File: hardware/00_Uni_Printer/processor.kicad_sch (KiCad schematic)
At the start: 31 parts, among them IC2 MT25QL256ABA1EW7-0SIT_TR, U1 STM32H743VIT6, U4 TLE9251VSJ, U7 LTC2862CS8-1#PBF, Y1 ABM7-25.000MHZ-D2Y-T

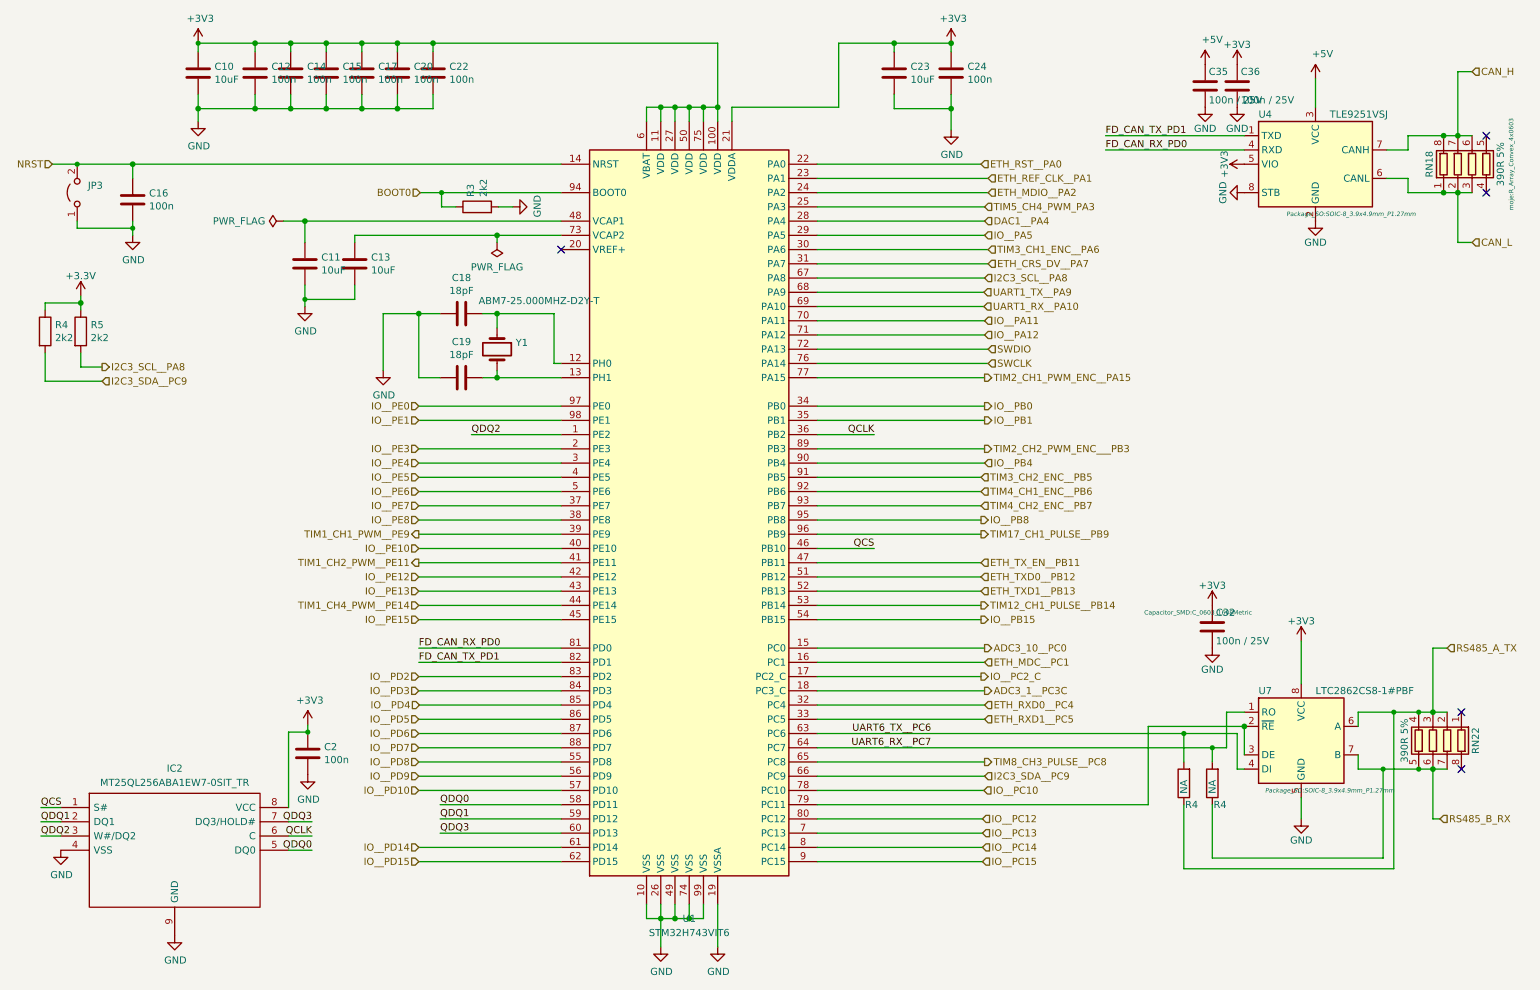
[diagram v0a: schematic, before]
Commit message: Removed CAN and RS485 drivers
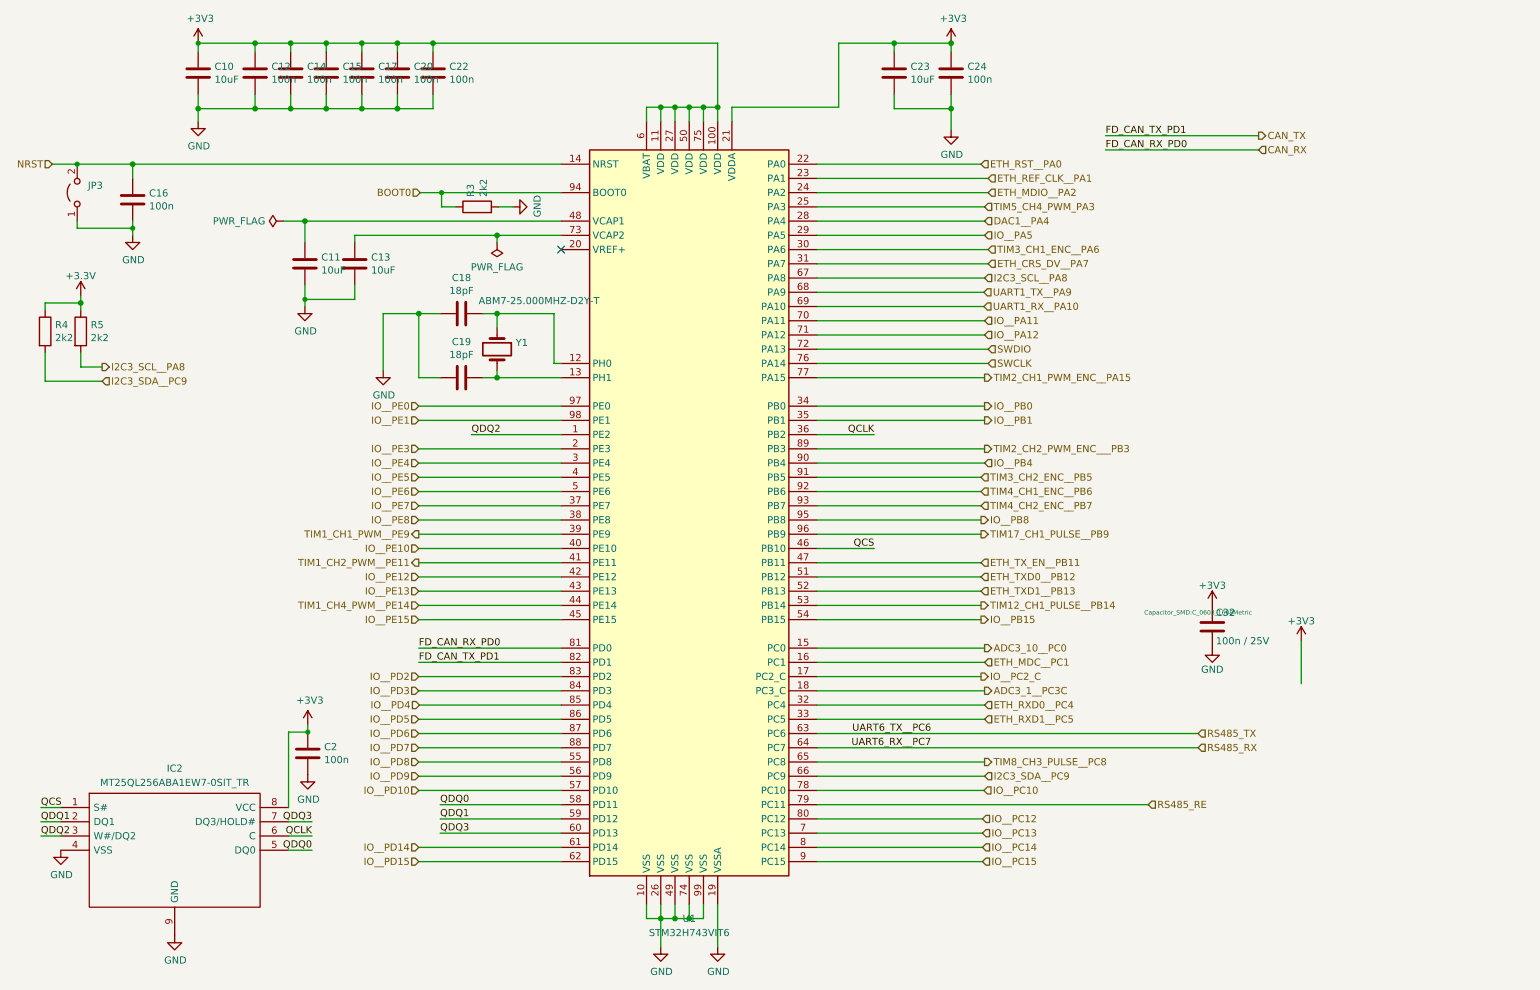
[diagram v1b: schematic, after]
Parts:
- removed C35, C36: 100n / 25V, Capacitor_SMD:C_0603_1608Metric, symbol mfc_base_lib:C
- removed R4 (x2): 2k2, Resistor_SMD:R_0603_1608Metric, symbol Uni_Printer-rescue:R-Device
- removed RN18, RN22: 390R 5%, moje:R_Array_Convex_4x0603, symbol mfc_base_lib:R_Pack04
- removed U4: TLE9251VSJ, Package_SO:SOIC-8_3.9x4.9mm_P1.27mm, symbol mfc_base_lib:TLE9251VSJ
- removed U7: LTC2862CS8-1#PBF, Package_SO:SOIC-8_3.9x4.9mm_P1.27mm, symbol mfc_base_lib:SP3481EN
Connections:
- net RS485_RE: now reaches U1.79 (PC11)
- net FD_CAN_RX_PD0 renamed CAN_RX
- net FD_CAN_TX_PD1 renamed CAN_TX
- net UART6_RX__PC7 renamed RS485_RX
- net UART6_TX__PC6 renamed RS485_TX
- no-connect marks 5 -> 1

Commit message: Fixes in PCB design
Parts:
- removed C32: 100n / 25V, Capacitor_SMD:C_0603_1608Metric, symbol mfc_base_lib:C
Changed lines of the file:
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@@
-    (stroke (width 0) (type solid) (color 0 0 0 0))
-  )
-  (wire (pts (xy 244.475 125.095) (xy 244.475 132.715))
     (stroke (width 0) (type solid) (color 0 0 0 0))
   )
@@
     (pin "1")
   )
-  (symbol (lib_id "mfc_base_lib:+3V3") (at 228.6 118.745 0) (unit 1)
-    (in_bom yes) (on_board yes)
-    (property "Reference" "#PWR0106" (id 0) (at 228.6 122.555 0)
-      (effects (font (size 1.27 1.27)) hide)
-    )
-    (property "Value" "+3V3" (id 1) (at 228.6 115.189 0))
-    (property "Footprint" "" (id 2) (at 228.6 118.745 0)
-      (effects (font (size 1.27 1.27)) hide)
-    )
-    (property "Datasheet" "" (id 3) (at 228.6 118.745 0)
-      (effects (font (size 1.27 1.27)) hide)
-    )
-    (pin "1")
-  )
   (symbol (lib_id "Jumper:Jumper_2_Open") (at 26.035 45.085 90) (unit 1)
     (in_bom yes) (on_board yes) (fields_autoplaced)
@@
     (property "Datasheet" "~" (id 3) (at 26.035 45.085 0)
       (effects (font (size 1.27 1.27)) hide)
-    )
-    (pin "1")
-    (pin "2")
-  )
-  (symbol (lib_id "mfc_base_lib:C") (at 228.6 122.555 0) (unit 1)
-    (in_bom yes) (on_board yes)
-    (property "Reference" "C32" (id 0) (at 229.235 120.015 0)
-      (effects (font (size 1.27 1.27)) (justify left))
-    )
-    (property "Value" "100n / 25V" (id 1) (at 229.235 125.095 0)
-      (effects (font (size 1.27 1.27)) (justify left))
-    )
-    (property "Footprint" "Capacitor_SMD:C_0603_1608Metric" (id 2) (at 226.06 120.015 0)
-      (effects (font (size 0.7874 0.7874)))
-    )
-    (property "Datasheet" "" (id 3) (at 228.6 122.555 0)
-      (effects (font (size 1.27 1.27)) hide)
-    )
-    (property "Category" "Capacitor" (id 4) (at 228.6 122.555 0)
-      (effects (font (size 1.524 1.524)) hide)
     )
     (pin "1")
@@
       (effects (font (size 1.27 1.27)) hide)
     )
-    (pin "1")
-  )
-  (symbol (lib_id "mfc_base_lib:+3V3") (at 244.475 125.095 0) (unit 1)
-    (in_bom yes) (on_board yes)
-    (property "Reference" "#PWR0103" (id 0) (at 244.475 128.905 0)
-      (effects (font (size 1.27 1.27)) hide)
-    )
-    (property "Value" "+3V3" (id 1) (at 244.475 121.539 0))
-    (property "Footprint" "" (id 2) (at 244.475 125.095 0)
-      (effects (font (size 1.27 1.27)) hide)
-    )
-    (property "Datasheet" "" (id 3) (at 244.475 125.095 0)
-      (effects (font (size 1.27 1.27)) hide)
-    )
-    (pin "1")
-  )
-  (symbol (lib_id "mfc_base_lib:GND") (at 228.6 126.365 0) (unit 1)
-    (in_bom yes) (on_board yes)
-    (property "Reference" "#PWR0102" (id 0) (at 228.6 132.715 0)
-      (effects (font (size 1.27 1.27)) hide)
-    )
-    (property "Value" "GND" (id 1) (at 228.6 130.175 0))
-    (property "Footprint" "" (id 2) (at 228.6 126.365 0)
-      (effects (font (size 1.27 1.27)) hide)
-    )
-    (property "Datasheet" "" (id 3) (at 228.6 126.365 0)
-      (effects (font (size 1.27 1.27)) hide)
-    )
